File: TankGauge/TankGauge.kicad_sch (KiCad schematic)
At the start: 18 parts, among them J1 Screw_Terminal_01x02, J2 Screw_Terminal_01x04, J3 Screw_Terminal_01x02, J4 Screw_Terminal_01x03, Q1 IRF540N, U1 LTC4365TS8, U2 TMP100

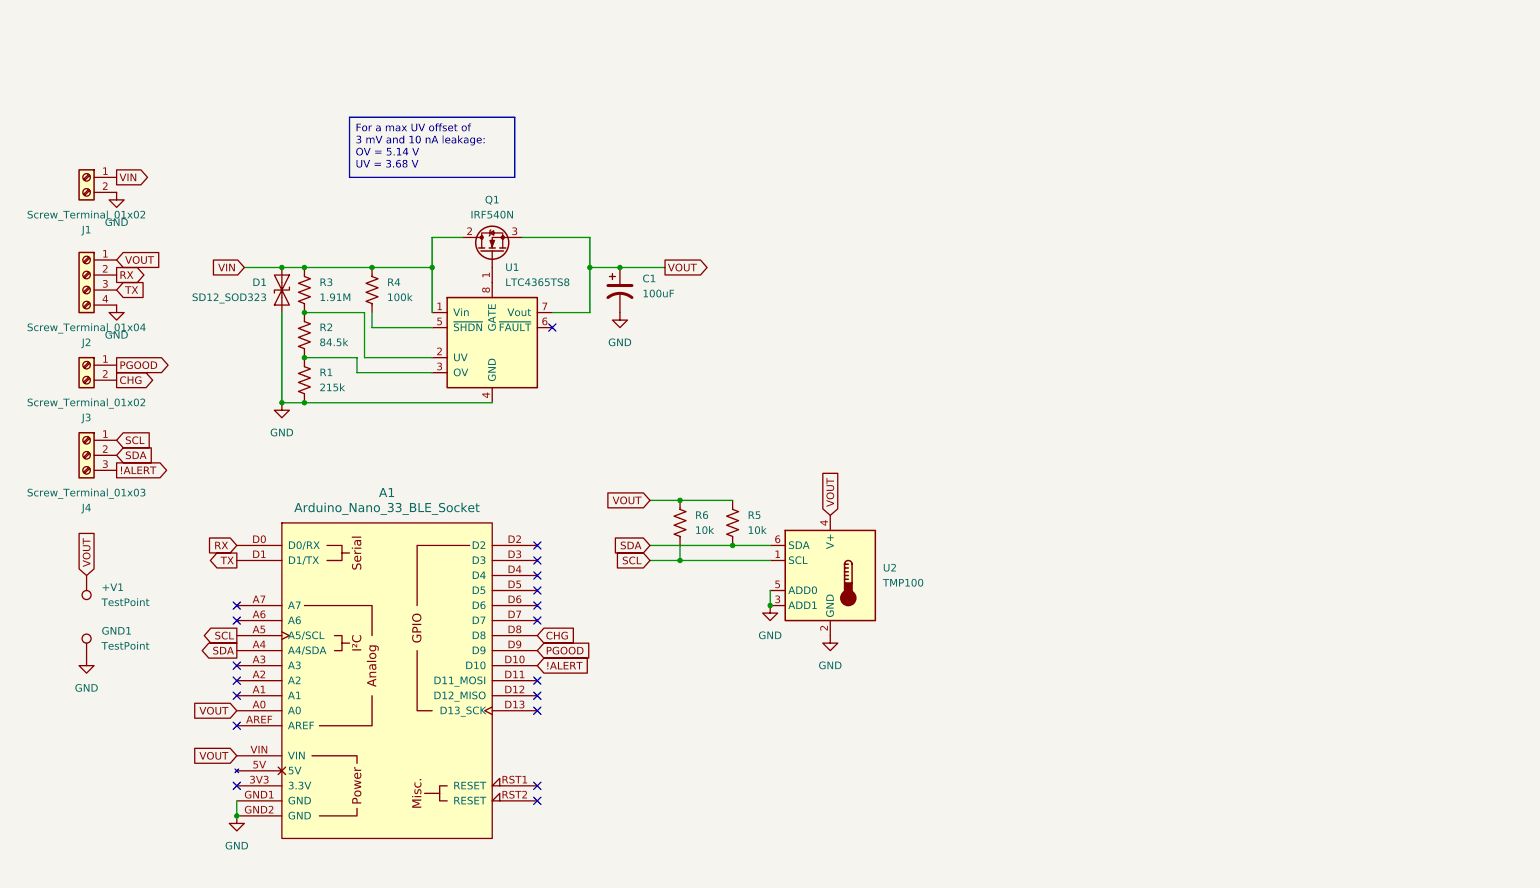
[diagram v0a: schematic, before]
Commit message: Added a voltage divider to address #1.
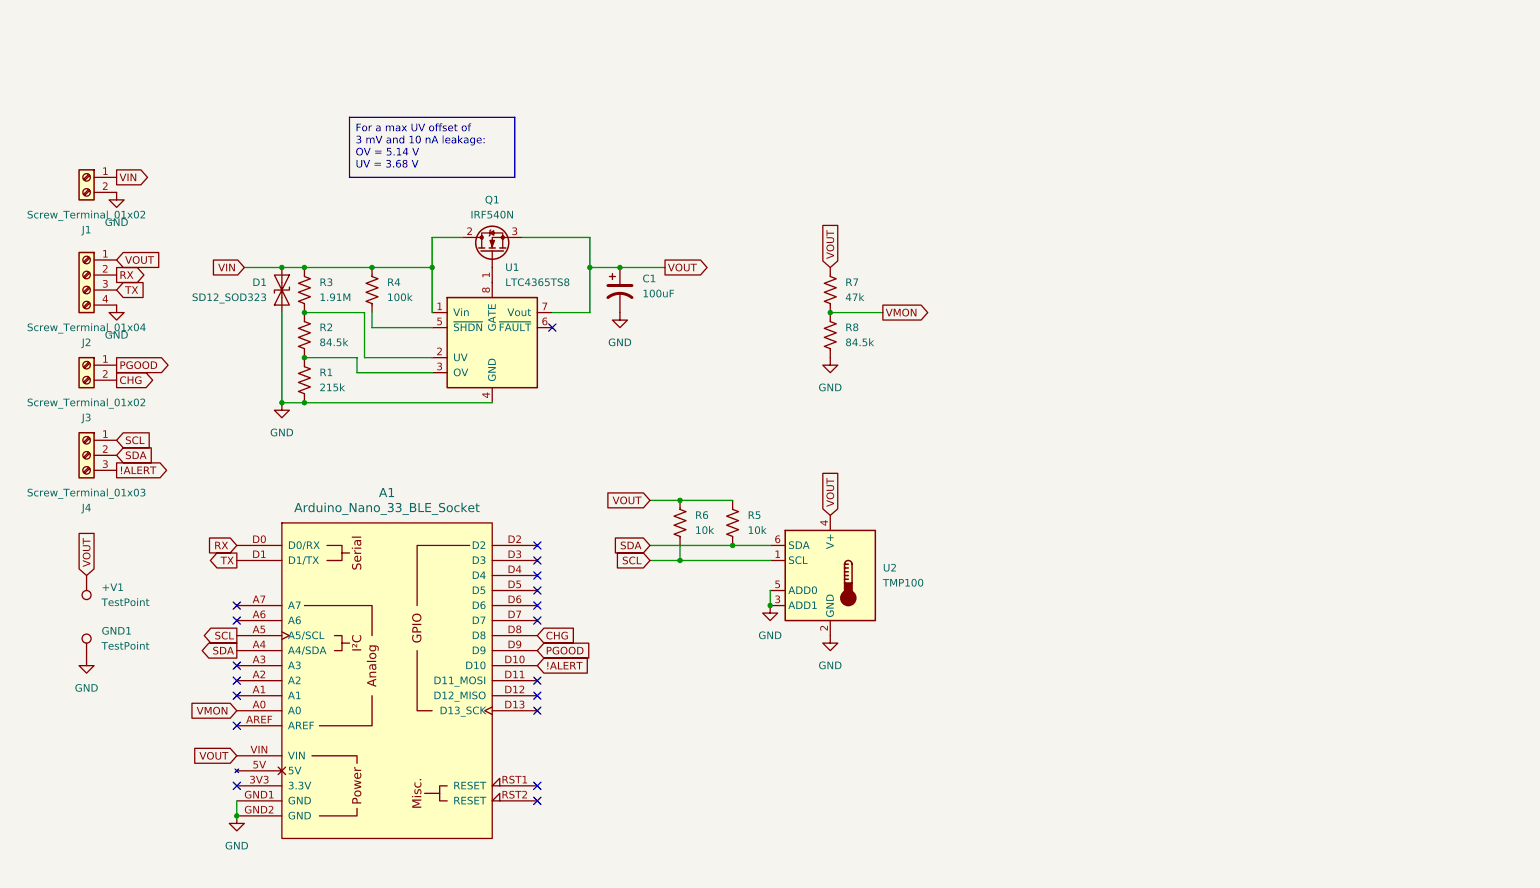
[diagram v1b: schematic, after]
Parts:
- added R7: 47k, Resistor_SMD:R_0805_2012Metric_Pad1.20x1.40mm_HandSolder, symbol Device:R_US
- added R8: 84.5k, Resistor_SMD:R_0805_2012Metric_Pad1.20x1.40mm_HandSolder, symbol Device:R_US
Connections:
- net GND: now also R8.2
- net VOUT: now also R7.1; no longer A1.A0
- new net VMON: A1.A0, R7.2, R8.1

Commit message: Use the eTape and a ADS1115 for better results.
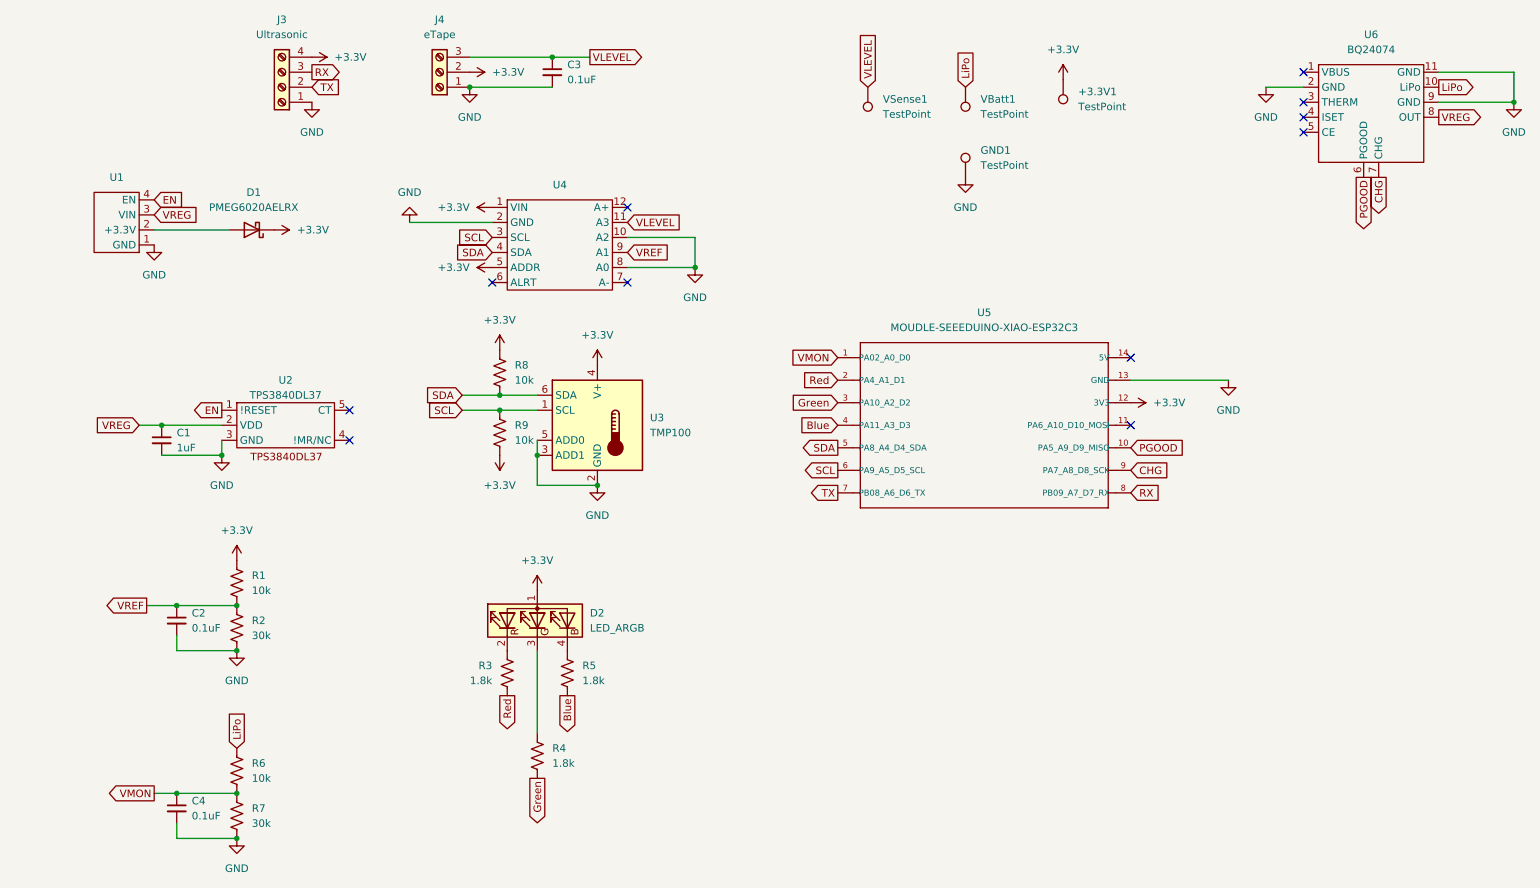
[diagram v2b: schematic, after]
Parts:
- removed +V1: TestPoint, TestPoint:TestPoint_Pad_D2.0mm, symbol Connector:TestPoint
- removed A1: Arduino_Nano_33_BLE_Socket, PCM_arduino-library:Arduino_Nano_Every_Socket, symbol Arduino:Arduino_Nano_33_BLE_Socket
- removed C1: 100uF, Capacitor_THT:CP_Radial_D6.3mm_P2.50mm, symbol Device:C_Polarized_US
- removed D1: SD12_SOD323, Diode_SMD:D_SOD-323, symbol Diode:SD12_SOD323
- removed J1, J3: Screw_Terminal_01x02, Connector_PinHeader_2.54mm:PinHeader_1x02_P2.54mm_Vertical, symbol Connector:Screw_Terminal_01x02
- removed J2: Screw_Terminal_01x04, Connector_PinHeader_2.54mm:PinHeader_1x04_P2.54mm_Vertical, symbol Connector:Screw_Terminal_01x04
- removed Q1: IRF540N, Package_TO_SOT_THT:TO-220-3_Vertical, symbol Transistor_FET:IRF540N
- removed U1: LTC4365TS8, Package_TO_SOT_SMD:TSOT-23-8, symbol Power_Management:LTC4365TS8
- added +3.3V1, VBatt1, VSense1: TestPoint, TestPoint:TestPoint_Pad_D2.0mm, symbol Connector:TestPoint
- added C1: 1uF, Capacitor_SMD:C_0805_2012Metric_Pad1.18x1.45mm_HandSolder, symbol Device:C_Small
- added C2, C3, C4: 0.1uF, Capacitor_SMD:C_0805_2012Metric_Pad1.18x1.45mm_HandSolder, symbol Device:C_Small
- added D1: PMEG6020AELRX, Diode_SMD:Nexperia_CFP3_SOD-123W, symbol Device:D_Schottky
- added D2: LED_ARGB, LED_SMD:LED_Kingbright_AAA3528ESGCT, symbol Device:LED_ARGB
- added J3: Ultrasonic, Connector_PinHeader_2.54mm:PinHeader_1x04_P2.54mm_Vertical, symbol Connector:Screw_Terminal_01x04
- added R9: 10k, Resistor_SMD:R_0805_2012Metric_Pad1.20x1.40mm_HandSolder, symbol Device:R_US
- added U1: TLV62569, Module:TLV62569 Breakout Board, symbol Regulator_Switching:TLV62569 Breakout Board
- added U2: TPS3840DL37, Package_TO_SOT_SMD:SOT-23-5_HandSoldering, symbol Power_Management:TPS3840DL37
- added U4: ~, Module:ADS1115 Breakout Board, symbol Analog_ADC:ADS1115_Breakout_Board
- added U5: MOUDLE-SEEEDUINO-XIAO-ESP32C3, Library:XIAO-ESP32C3, symbol MCU_Espressif:MOUDLE-SEEEDUINO-XIAO-ESP32C3
- added U6: BQ24074, Connector_PinHeader_2.54mm:PinHeader_1x11_P2.54mm_Vertical, symbol Battery_Management:BQ24072_Breakout_Board
- J4: value Screw_Terminal_01x03 -> eTape
- R1: value 215k -> 10k
- R2: value 84.5k -> 30k
- R3: value 1.91M -> 1.8k
- R4: value 100k -> 1.8k
- R5: value 10k -> 1.8k
- R7: value 47k -> 30k
- R8: value 84.5k -> 10k
- renumbered U2 to U3
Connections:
- net CHG: now also U5.9 (PA7_A8_D8_SCK), U6.7 (CHG)
- net GND: now also J4.1 (Pin_1), R2.2, R7.2, C1.2, C2.2, C3.2, C4.2, J3.1 (Pin_1), U1.1 (GND), U2.3 (GND), U4.10 (A2), U4.2 (GND), U4.8 (A0), U5.13 (GND), U6.11 (GND), U6.2 (GND), U6.9 (GND); no longer R1.2, R8.2
- net PGOOD: now also U5.10 (PA5_A9_D9_MISO), U6.6 (PGOOD)
- net RX: now also J3.3 (Pin_3), U5.8 (PB09_A7_D7_RX)
- net SCL: now also R9.1, U4.3 (SCL), U5.6 (PA9_A5_D5_SCL); no longer J4.1 (Pin_1), R6.2
- net SDA: now also R8.2, U4.4 (SDA), U5.5 (PA8_A4_D4_SDA); no longer J4.2 (Pin_2), R5.2
- net TX: now also J3.2 (Pin_2), U5.7 (PB08_A6_D6_TX)
- net VMON: now also R6.2, R7.1, C4.1, U5.1 (PA02_A0_D0); no longer R7.2, R8.1
- net Red: now reaches R3.2
- net Red: now also U5.2 (PA4_A1_D1); no longer R2.1
- net +3.3V: now reaches R1.1
- net +3.3V: now also J4.2 (Pin_2), R8.1, U3.4 (V+), +3.3V1.1, D1.1 (K), D2.1 (A), J3.4 (Pin_4), R9.2, U4.1 (VIN), U4.5 (ADDR), U5.12 (3V3); no longer R2.2
- net Green: now reaches R4.2
- net Green: now also U5.3 (PA10_A2_D2)
- net !ALERT renamed VLEVEL
- net VLEVEL: now also C3.1, U4.11 (A3), VSense1.1
- net VIN: no longer names the net of R3.1
- net VIN: now also D2.2 (RK); no longer R4.1
- removed net VOUT: R5.1, R6.1, R7.1, U3.4 (V+)
- new net: D2.4 (BK), R5.1
- new net: D2.3 (GK), R4.1
- new net: D1.2 (A), U1.2 (+3.3V)
- new net Blue: R5.2, U5.4 (PA11_A3_D3)
- new net EN: U1.4 (EN), U2.1 (!RESET)
- new net LiPo: R6.1, U6.10 (LiPo), VBatt1.1
- new net VREF: C2.1, R1.2, R2.1, U4.9 (A1)
- new net VREG: C1.1, U1.3 (VIN), U2.2 (VDD), U6.8 (OUT)
- no-connect marks 19 -> 11
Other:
- moved on the sheet: GND1, U3

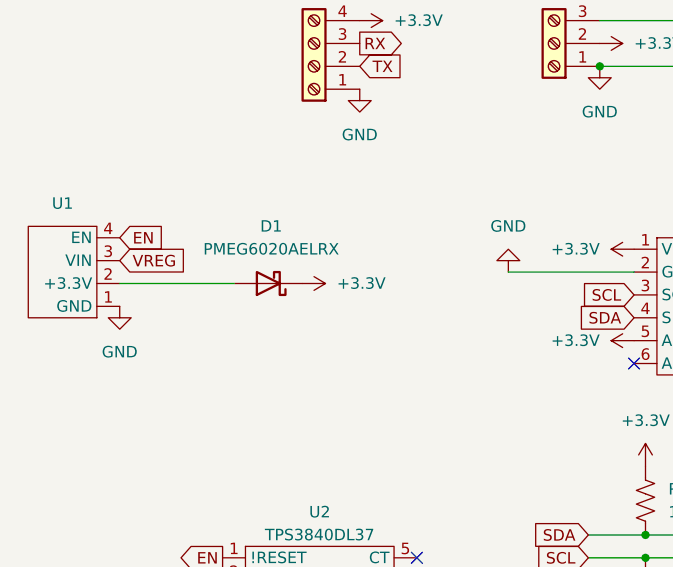
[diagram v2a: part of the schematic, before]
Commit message: DNP D1 since it has too much voltage drop across it.
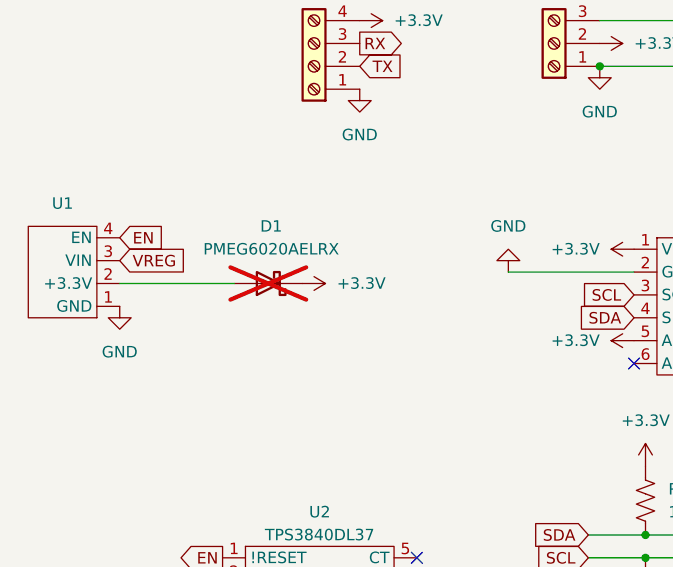
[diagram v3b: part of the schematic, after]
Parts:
- D1: now not fitted
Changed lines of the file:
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@@
 		(in_bom yes)
 		(on_board yes)
-		(dnp no)
+		(dnp yes)
 		(fields_autoplaced yes)
 		(property "Reference" "D1"

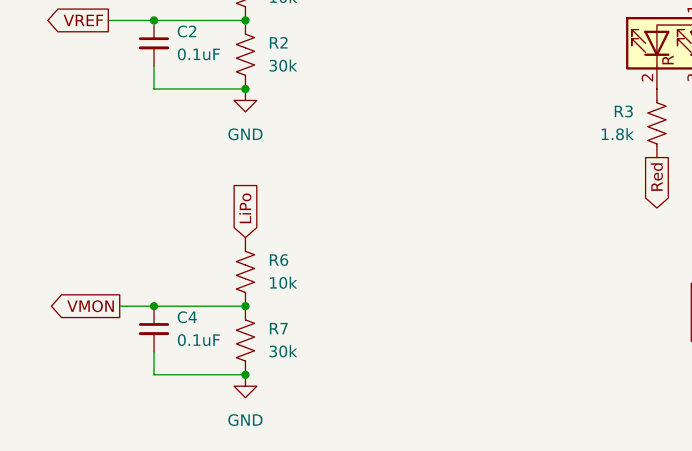
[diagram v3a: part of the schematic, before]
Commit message: Change voltage divider ratio on the battery monitor.
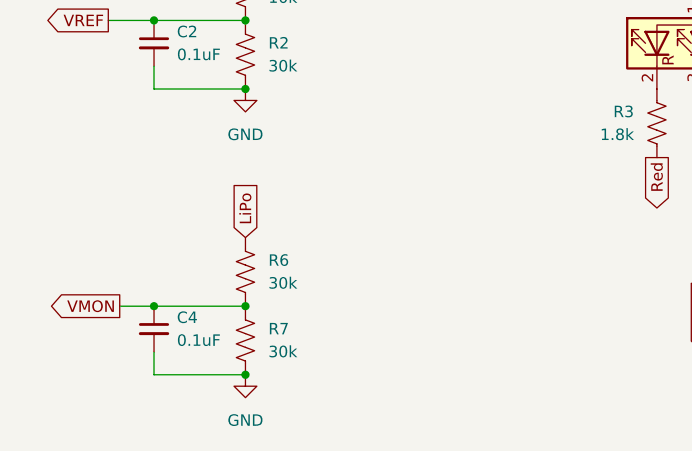
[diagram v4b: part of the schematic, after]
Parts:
- R6: value 10k -> 30k
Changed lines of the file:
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@@
 			)
 		)
-		(property "Value" "10k"
+		(property "Value" "30k"
 			(at 46.99 142.2399 0)
 			(effects
